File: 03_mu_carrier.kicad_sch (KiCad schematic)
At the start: 157 parts, among them J10 Amphenol MDT420M01001 M-key N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, J8 DNP Mu SIO UART debug header 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, Q750 BSS138 fail-off EN/UVLO clamp, Q751 BSS138 active-high enable rel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, SW2 Mu Power, SW3 Mu Reset, U6 TPS56637RPAR VSYS -> SYS_5V (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, U7 TPS56637RPAR VSYS -> SYS_3V3 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, U750 TPS552892RYQR 12V buck-boost, U769 SN74LVC1G08DBVR qualified hos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, U770 TPS2553DDBVR internal host VB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, U771 TPS3897ADRYR internal VBUS su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, U772 TPS22975NDSGR switched PCIe e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, U773 TPS56637RPAR VSYS -> PCIE_3V3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

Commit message: Independent-verifier sweep: fix 12 stale contracts + 4 real board bugs
The full independent verification suite (not just the schematic gate)
caught real issues before routing:

Contracts/verifiers fixed (9 stale expectations that would have masked
regressions):
- U44 pin 9: SOURCE_MGR_SPARE2 -> SLS_S3 (contracts + closure)
- U61 pins 1/3/7: GND/NC -> EC_DFU_SEL / DFU DP/DM (DFU rework)
- C832 + U772 pins 1/2/4: SYS_3V3 -> PCIE_3V3_IN (endpoint buck)
- J2300: full 60-pin -> verified 30-pin FH12 map (contracts + pin review)
- J9 RTC header block -> D1824/C783 diode-OR block
- U63/R203 obsolete expectations (refs reused for the DFU parts)

Real board bugs found and fixed:
- J11 right-edge USB-C misplaced 6 mm inside the edge (shell pad would
  never align with the chassis cutout); moved to mirror J12 at x 353.48
- R207 fan PWM series resistor stranded at the right edge (shorted
  J11's shell); relocated under the NVMe card (height-legal), clear of
  the charger/mux clusters
- C35 placed inside the Ethernet notch void (would be routed off);
  moved to x 348
- BOM: 11 new parts missing Manufacturer/MPN stamps -> catalog entries
  added; BOM gate now PASS (0 gaps)

Release gate now: DRC all allowlisted (courtyards 165, silk 8+1),
schematic parity 0, pin review 2575 PASS / 0 FAIL, closure 1605/0,
calcs 123/0, off-board anchors 0. Remaining FAILs are expected:
stackup PENDING_NEXTPCB (awaiting fab reply) and 499 unrouted.
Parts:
- C778: MPN (none) -> GRM188R71H104KA93D; Manufacturer (none) -> Murata
- C779: MPN (none) -> C1608X7R1C104K080AA; Manufacturer (none) -> TDK
- R779, R784, R787, R788: MPN (none) -> RC0603FR-07100KL; Manufacturer (none) -> Yageo
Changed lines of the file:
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@@
   (property "Footprint" "Resistor_SMD:R_0603_1608Metric" (at 39.37 110.49 0) (effects (font (size 1.27 1.27)) (hide yes)))
   (property "Datasheet" "" (at 39.37 110.49 0) (effects (font (size 1.27 1.27)) (hide yes)))
+  (property "Manufacturer" "Yageo" (at 39.37 110.49 0) (effects (font (size 1.27 1.27)) (hide yes)))
+  (property "MPN" "RC0603FR-07100KL" (at 39.37 110.49 0) (effects (font (size 1.27 1.27)) (hide yes)))
   (pin "1")
   (pin "2")
@@
   (property "Footprint" "Resistor_SMD:R_0603_1608Metric" (at 49.53 110.49 0) (effects (font (size 1.27 1.27)) (hide yes)))
   (property "Datasheet" "" (at 49.53 110.49 0) (effects (font (size 1.27 1.27)) (hide yes)))
+  (property "Manufacturer" "Yageo" (at 49.53 110.49 0) (effects (font (size 1.27 1.27)) (hide yes)))
+  (property "MPN" "RC0603FR-07100KL" (at 49.53 110.49 0) (effects (font (size 1.27 1.27)) (hide yes)))
   (pin "1")
   (pin "2")
@@
   (property "Footprint" "Capacitor_SMD:C_0603_1608Metric" (at 1029.97 420.37 0) (effects (font (size 1.27 1.27)) (hide yes)))
   (property "Datasheet" "" (at 1029.97 420.37 0) (effects (font (size 1.27 1.27)) (hide yes)))
+  (property "Manufacturer" "Murata" (at 1029.97 420.37 0) (effects (font (size 1.27 1.27)) (hide yes)))
+  (property "MPN" "GRM188R71H104KA93D" (at 1029.97 420.37 0) (effects (font (size 1.27 1.27)) (hide yes)))
   (pin "1")
   (pin "2")
@@
   (property "Footprint" "Capacitor_SMD:C_0603_1608Metric" (at 1040.13 420.37 0) (effects (font (size 1.27 1.27)) (hide yes)))
   (property "Datasheet" "" (at 1040.13 420.37 0) (effects (font (size 1.27 1.27)) (hide yes)))
+  (property "Manufacturer" "TDK" (at 1040.13 420.37 0) (effects (font (size 1.27 1.27)) (hide yes)))
+  (property "MPN" "C1608X7R1C104K080AA" (at 1040.13 420.37 0) (effects (font (size 1.27 1.27)) (hide yes)))
   (pin "1")
   (pin "2")
@@
   (property "Footprint" "Resistor_SMD:R_0603_1608Metric" (at 1040.13 439.42 0) (effects (font (size 1.27 1.27)) (hide yes)))
   (property "Datasheet" "" (at 1040.13 439.42 0) (effects (font (size 1.27 1.27)) (hide yes)))
+  (property "Manufacturer" "Yageo" (at 1040.13 439.42 0) (effects (font (size 1.27 1.27)) (hide yes)))
+  (property "MPN" "RC0603FR-07100KL" (at 1040.13 439.42 0) (effects (font (size 1.27 1.27)) (hide yes)))
   (pin "1")
   (pin "2")
@@
   (property "Footprint" "Resistor_SMD:R_0603_1608Metric" (at 1050.29 439.42 0) (effects (font (size 1.27 1.27)) (hide yes)))
   (property "Datasheet" "" (at 1050.29 439.42 0) (effects (font (size 1.27 1.27)) (hide yes)))
+  (property "Manufacturer" "Yageo" (at 1050.29 439.42 0) (effects (font (size 1.27 1.27)) (hide yes)))
+  (property "MPN" "RC0603FR-07100KL" (at 1050.29 439.42 0) (effects (font (size 1.27 1.27)) (hide yes)))
   (pin "1")
   (pin "2")

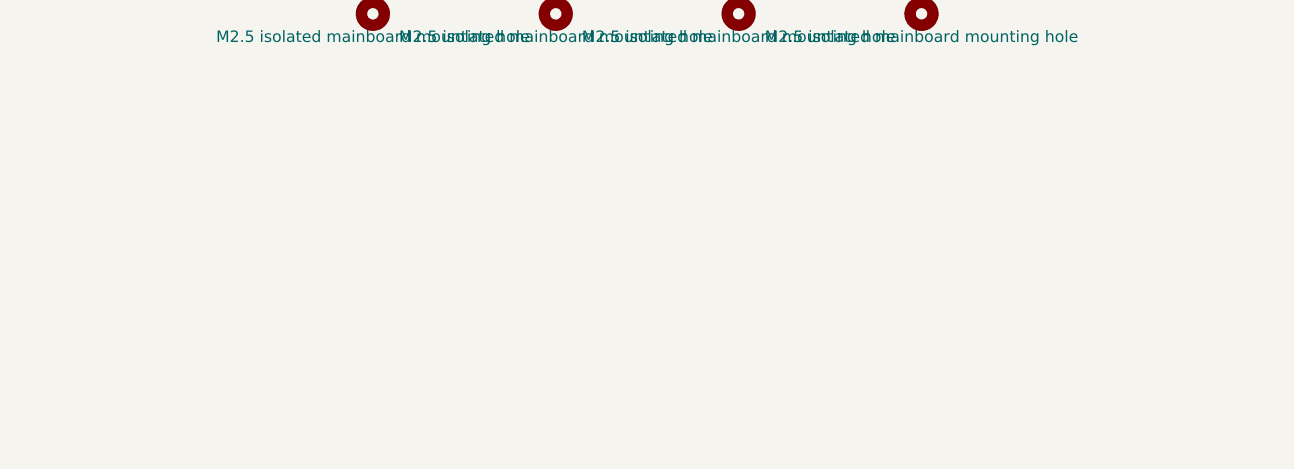
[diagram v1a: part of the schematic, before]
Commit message: Renumber duplicated mounting holes H21-H27; add schematic symbols
The user copy-pasted a mounting hole for extra chassis support; all
copies kept the H12 reference (8 duplicate footprints, parity 7).
Renumbered to H12 + H21-H27 (all positions kept), added matching
Mechanical:MountingHole symbols to the generator + regenerated the Mu
sheet (identity PASS), regenerated keepout zones for all 15 holes.

Parity now 0. DRC unchanged (only the user's in-progress placement
findings: 19 shorts / 6 clearances / courtyard+mask+silk deltas).
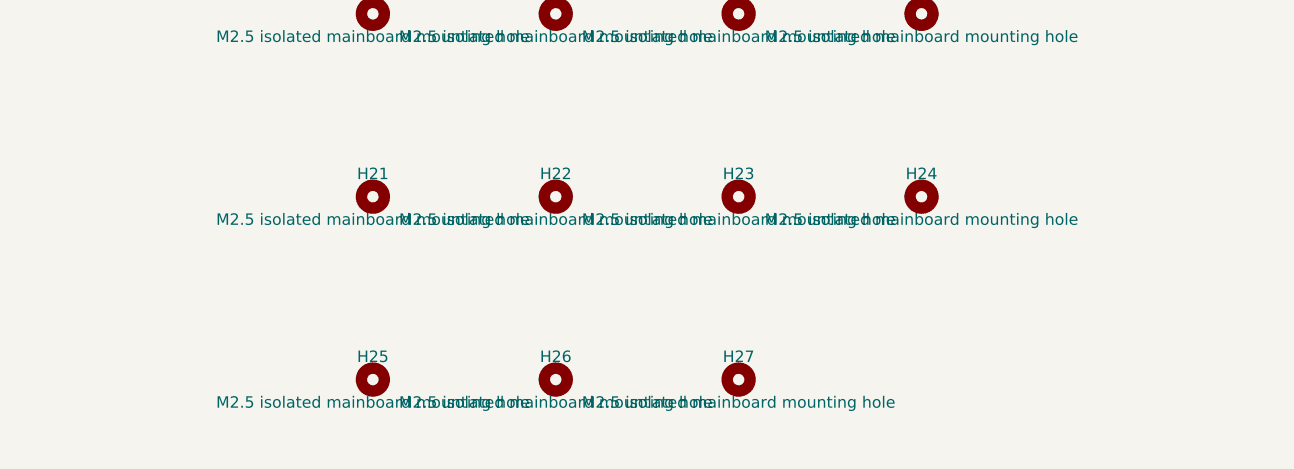
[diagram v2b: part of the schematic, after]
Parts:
- added H21, H22, H23, H24, H25, H26, H27: M2.5 isolated mainboard mounting hole, MountingHole:MountingHole_2.7mm_M2.5, symbol Mechanical:MountingHole
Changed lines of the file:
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@@
+  )
+)
+(symbol
+  (lib_id "Mechanical:MountingHole")
+  (at 599.44 640.08 0)
+  (unit 1)
+  (exclude_from_sim no)
+  (in_bom no)
+  (on_board yes)
+  (dnp no)
+  (property "Reference" "H21" (at 599.44 637.54 0) (effects (font (size 1.27 1.27))))
+  (property "Value" "M2.5 isolated mainboard mounting hole" (at 599.44 642.62 0) (effects (font (size 1.27 1.27))))
+  (property "Footprint" "MountingHole:MountingHole_2.7mm_M2.5" (at 599.44 640.08 0) (effects (font (size 1.27 1.27)) (hide yes)))
+  (property "Datasheet" "" (at 599.44 640.08 0) (effects (font (size 1.27 1.27)) (hide yes)))
+  (property "Hardware_Spec" "2.7mm isolated NPTH for M2.5 chassis screw; no electrical chassis bond" (at 599.44 640.08 0) (effects (font (size 1.27 1.27)) (hide yes)))
+  (instances
+    (project "ducktop2"
+      (path "/7f3572a2-a529-5ef0-93eb-27f85c0119a9"
+        (reference "H21")
+        (unit 1)
+      )
+    )
+  )
+)
+(symbol
+  (lib_id "Mechanical:MountingHole")
+  (at 619.76 640.08 0)
+  (unit 1)
+  (exclude_from_sim no)
+  (in_bom no)
+  (on_board yes)
+  (dnp no)
+  (property "Reference" "H22" (at 619.76 637.54 0) (effects (font (size 1.27 1.27))))
+  (property "Value" "M2.5 isolated mainboard mounting hole" (at 619.76 642.62 0) (effects (font (size 1.27 1.27))))
+  (property "Footprint" "MountingHole:MountingHole_2.7mm_M2.5" (at 619.76 640.08 0) (effects (font (size 1.27 1.27)) (hide yes)))
+  (property "Datasheet" "" (at 619.76 640.08 0) (effects (font (size 1.27 1.27)) (hide yes)))
+  (property "Hardware_Spec" "2.7mm isolated NPTH for M2.5 chassis screw; no electrical chassis bond" (at 619.76 640.08 0) (effects (font (size 1.27 1.27)) (hide yes)))
+  (instances
+    (project "ducktop2"
+      (path "/7f3572a2-a529-5ef0-93eb-27f85c0119a9"
+        (reference "H22")
+        (unit 1)
+      )
+    )
+  )
+)
+(symbol
+  (lib_id "Mechanical:MountingHole")
+  (at 640.08 640.08 0)
+  (unit 1)
+  (exclude_from_sim no)
+  (in_bom no)
+  (on_board yes)
+  (dnp no)
+  (property "Reference" "H23" (at 640.08 637.54 0) (effects (font (size 1.27 1.27))))
+  (property "Value" "M2.5 isolated mainboard mounting hole" (at 640.08 642.62 0) (effects (font (size 1.27 1.27))))
+  (property "Footprint" "MountingHole:MountingHole_2.7mm_M2.5" (at 640.08 640.08 0) (effects (font (size 1.27 1.27)) (hide yes)))
+  (property "Datasheet" "" (at 640.08 640.08 0) (effects (font (size 1.27 1.27)) (hide yes)))
+  (property "Hardware_Spec" "2.7mm isolated NPTH for M2.5 chassis screw; no electrical chassis bond" (at 640.08 640.08 0) (effects (font (size 1.27 1.27)) (hide yes)))
+  (instances
+    (project "ducktop2"
+      (path "/7f3572a2-a529-5ef0-93eb-27f85c0119a9"
+        (reference "H23")
+        (unit 1)
+      )
+    )
+  )
+)
+(symbol
+  (lib_id "Mechanical:MountingHole")
+  (at 660.4 640.08 0)
+  (unit 1)
+  (exclude_from_sim no)
+  (in_bom no)
+  (on_board yes)
+  (dnp no)
+  (property "Reference" "H24" (at 660.4 637.54 0) (effects (font (size 1.27 1.27))))
+  (property "Value" "M2.5 isolated mainboard mounting hole" (at 660.4 642.62 0) (effects (font (size 1.27 1.27))))
+  (property "Footprint" "MountingHole:MountingHole_2.7mm_M2.5" (at 660.4 640.08 0) (effects (font (size 1.27 1.27)) (hide yes)))
+  (property "Datasheet" "" (at 660.4 640.08 0) (effects (font (size 1.27 1.27)) (hide yes)))
+  (property "Hardware_Spec" "2.7mm isolated NPTH for M2.5 chassis screw; no electrical chassis bond" (at 660.4 640.08 0) (effects (font (size 1.27 1.27)) (hide yes)))
+  (instances
+    (project "ducktop2"
+      (path "/7f3572a2-a529-5ef0-93eb-27f85c0119a9"
+        (reference "H24")
+        (unit 1)
+      )
+    )
+  )
+)
+(symbol
+  (lib_id "Mechanical:MountingHole")
+  (at 599.44 660.4 0)
+  (unit 1)
+  (exclude_from_sim no)
+  (in_bom no)
+  (on_board yes)
+  (dnp no)
+  (property "Reference" "H25" (at 599.44 657.86 0) (effects (font (size 1.27 1.27))))
+  (property "Value" "M2.5 isolated mainboard mounting hole" (at 599.44 662.94 0) (effects (font (size 1.27 1.27))))
+  (property "Footprint" "MountingHole:MountingHole_2.7mm_M2.5" (at 599.44 660.4 0) (effects (font (size 1.27 1.27)) (hide yes)))
+  (property "Datasheet" "" (at 599.44 660.4 0) (effects (font (size 1.27 1.27)) (hide yes)))
+  (property "Hardware_Spec" "2.7mm isolated NPTH for M2.5 chassis screw; no electrical chassis bond" (at 599.44 660.4 0) (effects (font (size 1.27 1.27)) (hide yes)))
+  (instances
+    (project "ducktop2"
+      (path "/7f3572a2-a529-5ef0-93eb-27f85c0119a9"
+        (reference "H25")
+        (unit 1)
+      )
+    )
+  )
+)
+(symbol
+  (lib_id "Mechanical:MountingHole")
+  (at 619.76 660.4 0)
+  (unit 1)
+  (exclude_from_sim no)
+  (in_bom no)
+  (on_board yes)
+  (dnp no)
+  (property "Reference" "H26" (at 619.76 657.86 0) (effects (font (size 1.27 1.27))))
+  (property "Value" "M2.5 isolated mainboard mounting hole" (at 619.76 662.94 0) (effects (font (size 1.27 1.27))))
+  (property "Footprint" "MountingHole:MountingHole_2.7mm_M2.5" (at 619.76 660.4 0) (effects (font (size 1.27 1.27)) (hide yes)))
+  (property "Datasheet" "" (at 619.76 660.4 0) (effects (font (size 1.27 1.27)) (hide yes)))
+  (property "Hardware_Spec" "2.7mm isolated NPTH for M2.5 chassis screw; no electrical chassis bond" (at 619.76 660.4 0) (effects (font (size 1.27 1.27)) (hide yes)))
+  (instances
+    (project "ducktop2"
+      (path "/7f3572a2-a529-5ef0-93eb-27f85c0119a9"
+        (reference "H26")
+        (unit 1)
+      )
+    )
+  )
+)
+(symbol
+  (lib_id "Mechanical:MountingHole")
+  (at 640.08 660.4 0)
+  (unit 1)
+  (exclude_from_sim no)
+  (in_bom no)
+  (on_board yes)
+  (dnp no)
+  (property "Reference" "H27" (at 640.08 657.86 0) (effects (font (size 1.27 1.27))))
+  (property "Value" "M2.5 isolated mainboard mounting hole" (at 640.08 662.94 0) (effects (font (size 1.27 1.27))))
+  (property "Footprint" "MountingHole:MountingHole_2.7mm_M2.5" (at 640.08 660.4 0) (effects (font (size 1.27 1.27)) (hide yes)))
+  (property "Datasheet" "" (at 640.08 660.4 0) (effects (font (size 1.27 1.27)) (hide yes)))
+  (property "Hardware_Spec" "2.7mm isolated NPTH for M2.5 chassis screw; no electrical chassis bond" (at 640.08 660.4 0) (effects (font (size 1.27 1.27)) (hide yes)))
+  (instances
+    (project "ducktop2"
+      (path "/7f3572a2-a529-5ef0-93eb-27f85c0119a9"
+        (reference "H27")
+        (unit 1)
+      )
+    )
   )
 )

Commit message: Phase 5: second-opinion audit remediation + rebuilt, verified board pipeline
Second-opinion AI audit found A-tier defects; remediation applied and the
board pipeline rebuilt on a known-good base with the fixes it needed:

- electrical: LTC4418IUF symbol pinout corrected (both selectors were
  dead as drawn); center charge cascade (U15 <- U15B, PD1 > PD2 > AUX);
  pack negative never crosses FPC-3, 15-pin FG_VSS return; power-budgeted
  FPC pin maps (0.4 A/pin derate); J12/DS4 completed; AUX source fuse
- FH41-68S footprint: 13 datasheet-correct SH pads + SH pin in symbol
- connector geometry settled against the Hirose FH12 2D drawing: FFC
  enters opposite the solder pins (mouth = local +Y); reversed side-B
  maps are correct for the 180-deg-mounted pairs; rotations set so mouths
  face across every seam
- pipeline (generate_split_boards.py): per-pin pad-net resync from the
  netlists (kills shadow nets for good), netlist-exact name
  normalization, netlist-only part injection (cascade, probe headers),
  zone refill after outline swap, read-before-write race fixed, orphan
  parts dropped loudly, non-zero exit on unresolved overlaps
- monolith board relocated to old/monolith_ducktop2.kicad_pcb (placement
  oracle for the center cut only)

verified end state: 4 boards 0 shorts / 0 clearance / 0 drill, 0 boundary
crossings, 6/6 connectors contract-exact with mouths facing, 0 shadow
nets, gates PASS x4, ERC 0 x4. routing next (499 nets/board).
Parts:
- removed A2: DFR1149 LattePanda Mu N305 16GB/64GB removable mo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, symbol Mechanical:MountingHole
- removed H17, H21, H22, H23, H24, H25, H26, H27: M2.5 isolated mainboard mounting hole, MountingHole:MountingHole_2.7mm_M2.5, symbol Mechanical:MountingHole
- R40: value 76.8k 0.1% TPS56637 FB high -> 75.0k 0.1% TPS56637 FB high; MPN RT0603BRD0776K8L -> RT0603BRD075KL
- renumbered H10 to H14, H11 to H21, H12 to H22, H13 to H23, H14 to H24, H15 to H25, H16 to H26
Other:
- note added: "A2 = DFR1149 LattePanda Mu N305 16GB/64GB removable module (not a board part)"
- moved on the sheet: H14, H21, H22, H23, H24, H25, H26
